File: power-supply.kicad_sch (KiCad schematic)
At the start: 17 parts, among them Q1 SIA906EDJ-T1-GE3, U3 ADP5054ACPZ-R7, U4 ADP5050ACPZ-R7

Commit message: FPGA power supply WIP
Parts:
- added C?: C_22u_0603, antmicro-footprints:0603-cap, symbol antmicroCapacitors0603:C_22u_0603
- added C?: C_100n_0402, antmicro-footprints:0402-cap, symbol antmicroCapacitors0402:C_100n_0402
- added L?: XFL4020-472MEC, antmicro-footprints:XFL4020-102MEB, symbol antmicroFixedInductors:XFL4020-472MEC
- added R?: R_100k_0402, antmicro-footprints:0402-res, symbol antmicroResistors0402:R_100k_0402
- added R?: R_2k55_0402, antmicro-footprints:0402-res, symbol antmicroResistors0402:R_2k55_0402
- added R?: R_10k2_0402, antmicro-footprints:0402-res, symbol antmicroResistors0402:R_10k2_0402
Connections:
- net GND: now also U4.11 (PGND4), U4.2 (PGND3), U4.30 (PGND), U4.HTAB (EPAD), C?.2, R?.1
- net at U4.10 (SW4): now also C?.1, L?.1 (P)
- net at U4.12 (BST4): now also C?.2
- net at U4.16 (FB4): now also R?.2, R?.2
- new net: C?.1, L?.2 (P), R?.1
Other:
- moved on the sheet: U3

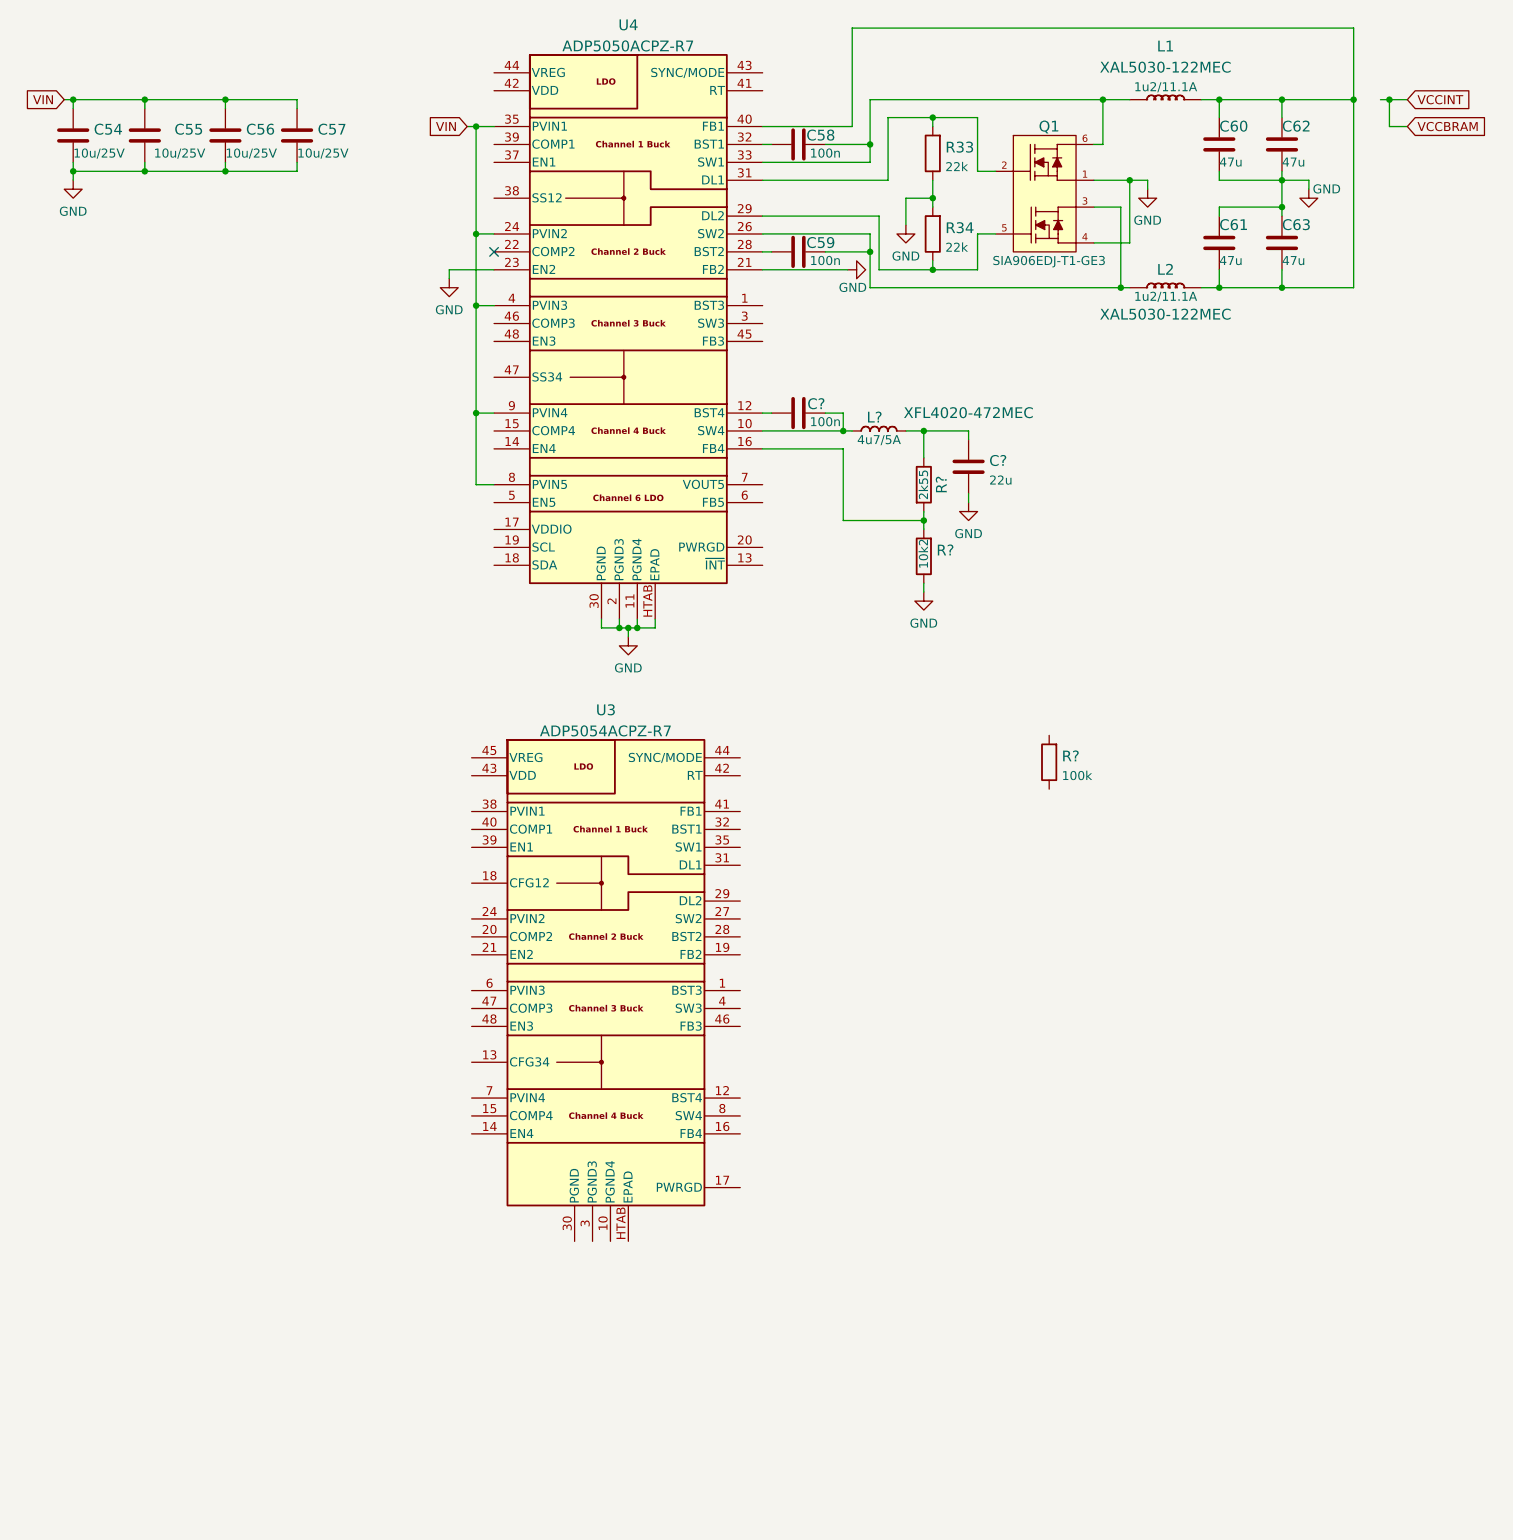
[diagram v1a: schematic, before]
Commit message: Add FPGA planar decoupling, finish DC-DC for 1V2, 1V35, 1V8, 3V3 and MGTAVCC rails
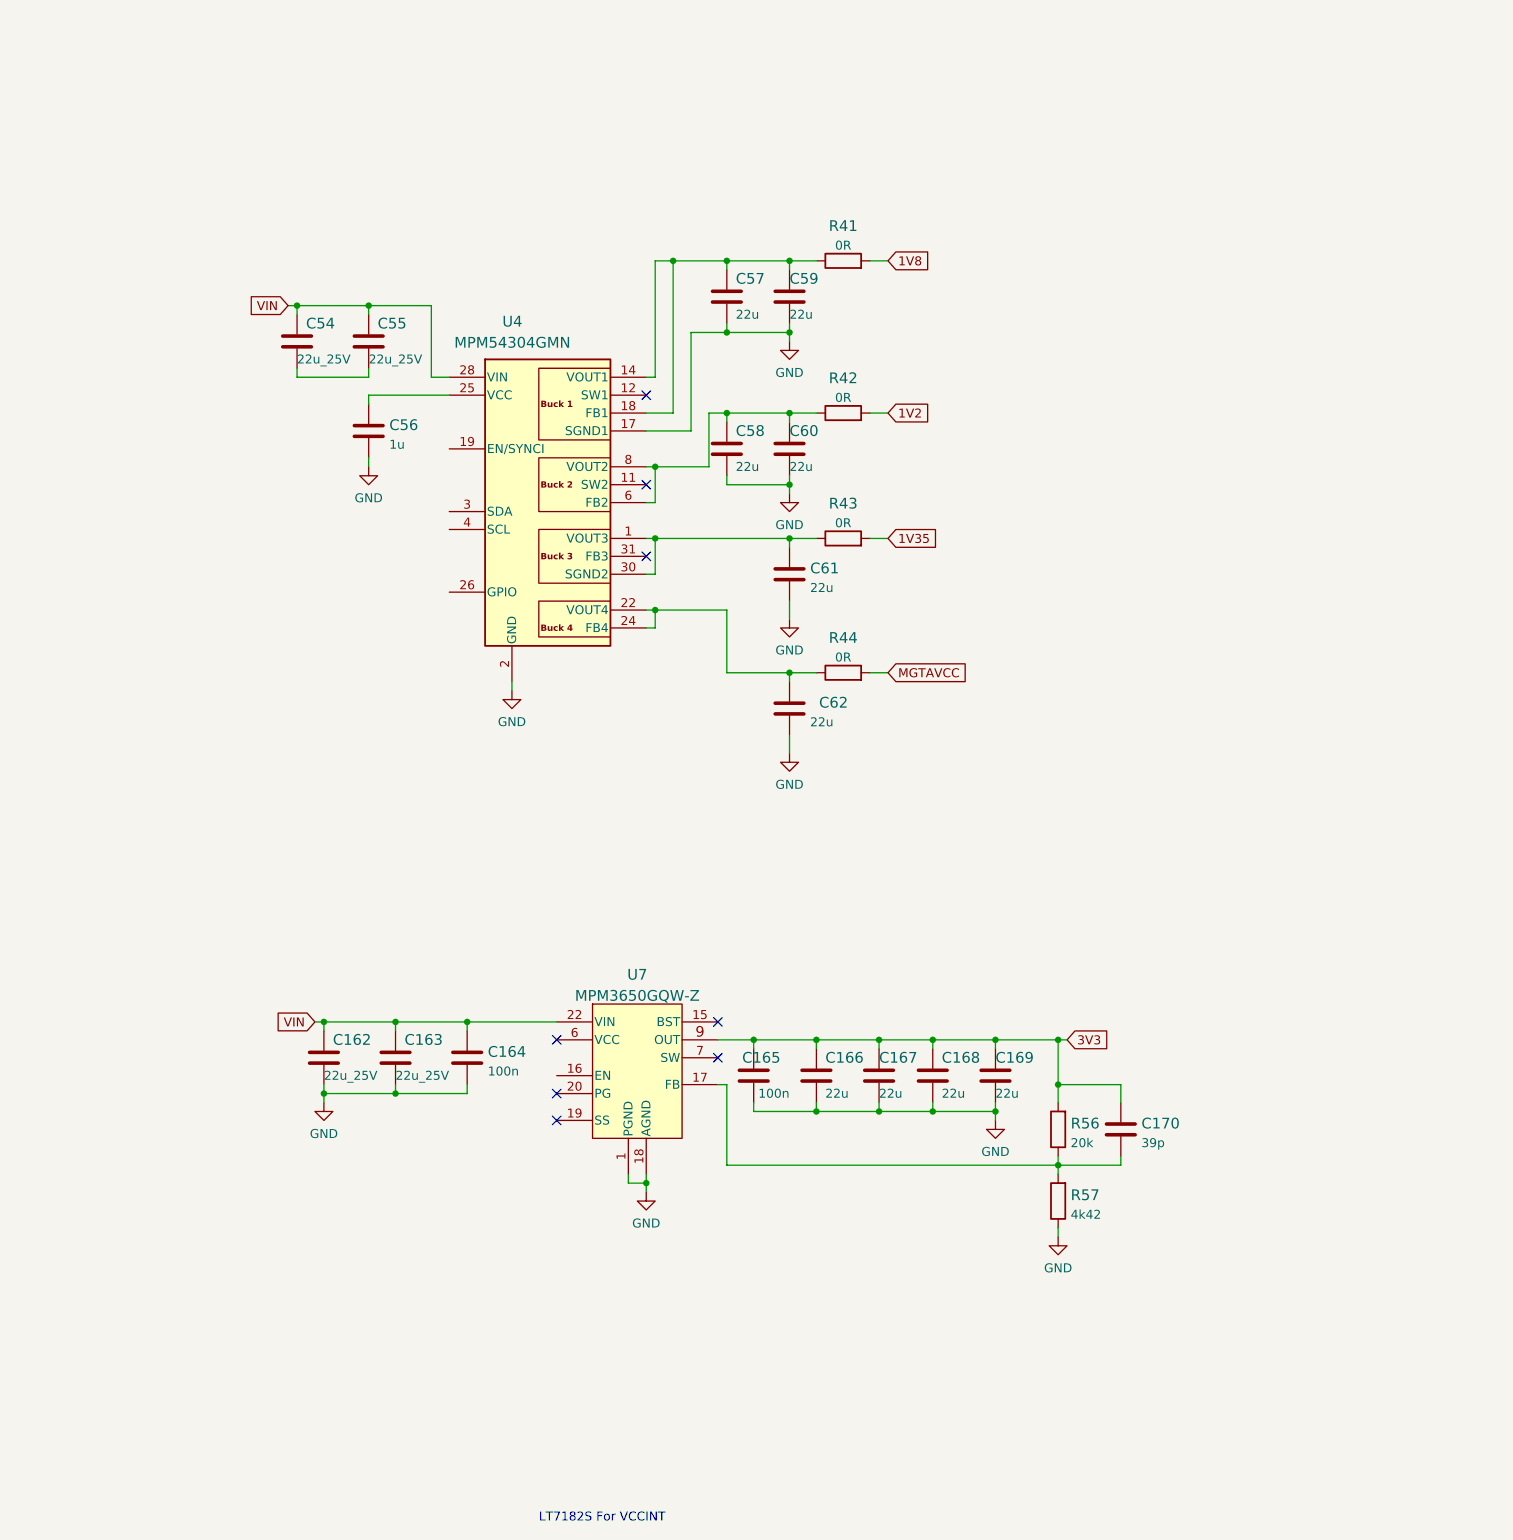
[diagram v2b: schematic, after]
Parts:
- removed C54, C55, C56, C57: C_10u_25V_0603, antmicro-footprints:0603-cap, symbol antmicroCapacitors0603:C_10u_25V_0603
- removed C58, C59, C?: C_100n_0402, antmicro-footprints:0402-cap, symbol antmicroCapacitors0402:C_100n_0402
- removed C60, C61, C62, C63: C_47u_0603, antmicro-footprints:0603-cap, symbol antmicroCapacitors0603:C_47u_0603
- removed C?: C_22u_0603, antmicro-footprints:0603-cap, symbol antmicroCapacitors0603:C_22u_0603
- removed L1, L2: XAL5030-122MEC, antmicro-footprints:Coilcraft-XAL5030, symbol antmicroFixedInductors:XAL5030-122MEC
- removed L?: XFL4020-472MEC, antmicro-footprints:XFL4020-102MEB, symbol antmicroFixedInductors:XFL4020-472MEC
- removed Q1: SIA906EDJ-T1-GE3, antmicro-footprints:VISHAY_PowerPAK_SC70-6L, symbol antmicroTransistorsFETsMOSFETsArrays:SIA906EDJ-T1-GE3
- removed R33, R34: R_22k_0402, antmicro-footprints:0402-res, symbol antmicroResistors0402:R_22k_0402
- removed R?: R_100k_0402, antmicro-footprints:0402-res, symbol antmicroResistors0402:R_100k_0402
- removed R?: R_2k55_0402, antmicro-footprints:0402-res, symbol antmicroResistors0402:R_2k55_0402
- removed R?: R_10k2_0402, antmicro-footprints:0402-res, symbol antmicroResistors0402:R_10k2_0402
- removed U3: ADP5054ACPZ-R7, antmicro-footprints:Analog_CP_48_13, symbol antmicroPMICVoltageRegulatorsDCDCSwitchingRegulators:ADP5054ACPZ-R7
- removed U4: ADP5050ACPZ-R7, antmicro-footprints:Analog_CP_48_13, symbol antmicroPMICVoltageRegulatorsDCDCSwitchingRegulators:ADP5050ACPZ-R7
- added C162, C163, C54, C55: C_22u_0805_25V, antmicro-footprints:0805-cap, symbol antmicroCapacitorsmisc:C_22u_0805_25V
- added C164, C165: C_100n_0402, antmicro-footprints:0402-cap, symbol antmicroCapacitors0402:C_100n_0402
- added C166, C167, C168, C169, C57, C58, C59, C60, C61, C62: C_22u_0603, antmicro-footprints:0603-cap, symbol antmicroCapacitors0603:C_22u_0603
- added C170: C_39p_0402, antmicro-footprints:0402-cap, symbol antmicroCapacitors0402:C_39p_0402
- added C56: C_1u_0402, antmicro-footprints:0402-cap, symbol antmicroCapacitors0402:C_1u_0402
- added R41, R42, R43, R44: R_0R_0805, antmicro-footprints:0805-res, symbol antmicroResistorsmisc:R_0R_0805
- added R56: R_20k_0402, antmicro-footprints:0402-res, symbol antmicroResistors0402:R_20k_0402
- added R57: R_4k42_0402, antmicro-footprints:0402-res, symbol antmicroResistors0402:R_4k42_0402
- added U4: MPM54304GMN, antmicro-footprints:MPS_LGA-33, symbol antmicroPMICVoltageRegulatorsDCDCSwitchingRegulators:MPM54304GMN
- added U7: MPM3650GQW-Z, antmicro-footprints:MPS_QFN24, symbol antmicroPMICVoltageRegulatorsDCDCSwitchingRegulators:MPM3650GQW-Z
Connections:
- net GND: now also C162.2, C163.2, C164.2, C165.2, C166.2, C167.2, C168.2, C169.2, C56.2, C57.2, C58.2, C59.2, C60.2, C61.2, C62.2, R57.1, U4.10 (GND), U4.13 (GND), U4.16 (GND), U4.17 (SGND1), U4.2 (GND), U4.20 (GND), U4.21 (GND), U4.27 (GND), U4.33 (GND), U4.5 (GND), U4.7 (GND), U7.1 (PGND), U7.18 (AGND), U7.2 (PGND), U7.24 (PGND), U7.3 (PGND), U7.4 (PGND), U7.5 (PGND)
- net VIN: now also C162.1, C163.1, C164.1, C54.1, C55.1, U4.28 (VIN), U4.29 (VIN), U7.22 (VIN)
- new net: C61.1, R43.1, U4.1 (VOUT3), U4.30 (SGND2), U4.32 (VOUT3)
- new net: C56.1, U4.25 (VCC)
- new net: C170.2, R56.1, R57.2, U7.17 (FB)
- new net: U7.13 (SW), U7.14 (SW), U7.23 (SW), U7.7 (SW), U7.8 (SW)
- new net: U7.20 (PG), U7.21 (PG)
- new net: C54.2, C55.2
- new net 1V2: R42.2
- new net 1V35: R43.2
- new net 1V8: R41.2
- new net 3V3: C165.1, C166.1, C167.1, C168.1, C169.1, C170.1, R56.2, U7.10 (OUT), U7.11 (OUT), U7.12 (OUT), U7.9 (OUT)
- new net MGTAVCC: R44.2
- new net VOUT1: C57.1, C59.1, R41.1, U4.14 (VOUT1), U4.15 (VOUT1), U4.18 (FB1)
- new net VOUT2: C58.1, C60.1, R42.1, U4.6 (FB2), U4.8 (VOUT2), U4.9 (VOUT2)
- new net VOUT4: C62.1, R44.1, U4.22 (VOUT4), U4.23 (VOUT4), U4.24 (FB4)
- no-connect marks 1 -> 8
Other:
- note added: "LT7182S For VCCINT"

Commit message: Unify sheets tables, add user-gpio sheet
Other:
- title: (none) -> K410T devboard
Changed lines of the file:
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@@
 (kicad_sch (version 20211123) (generator eeschema)
   (paper "A3")
+  (title_block
+    (title "K410T devboard")
+    (date "2022-12-20")
+    (rev "0.0.99")
+  )
   (junction (at 127 97.79) (diameter 0) (color 0 0 0 0)
   )

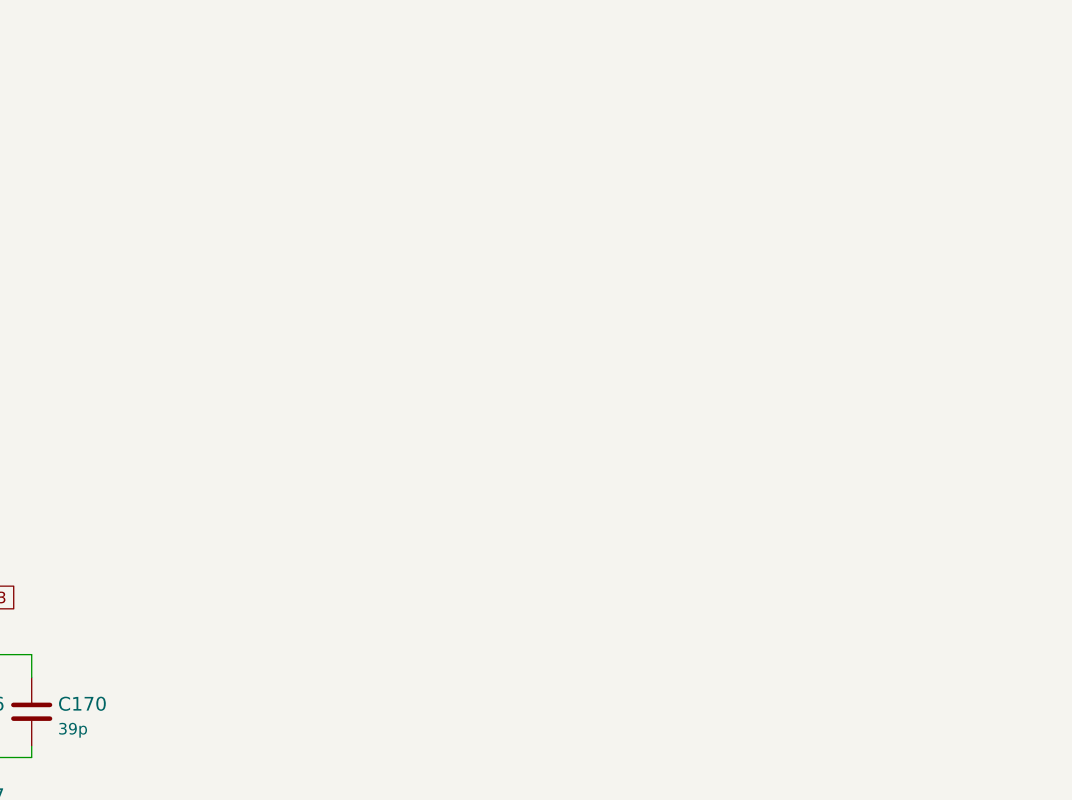
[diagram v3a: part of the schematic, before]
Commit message: Add DDR3L VTT termination regulator
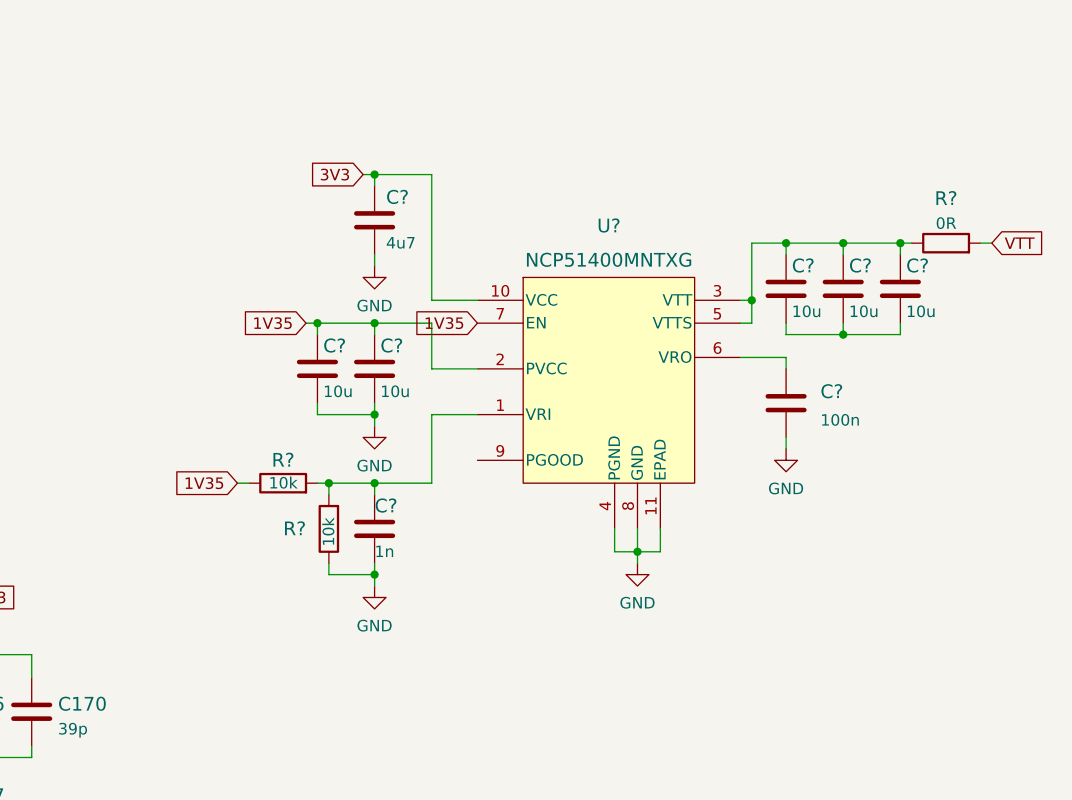
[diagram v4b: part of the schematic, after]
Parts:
- added C?: C_100n_0402, antmicro-footprints:0402-cap, symbol antmicroCapacitors0402:C_100n_0402
- added C? (x5): C_10u_0402, antmicro-footprints:0402-cap, symbol antmicroCapacitors0402:C_10u_0402
- added C?: C_4u7_0402, antmicro-footprints:0402-cap, symbol antmicroCapacitors0402:C_4u7_0402
- added C?: C_1n_0402, antmicro-footprints:0402-res, symbol antmicroCapacitors0402:C_1n_0402
- added R? (x2): R_10k_0402, antmicro-footprints:0402-res, symbol antmicroResistors0402:R_10k_0402
- added R?: R_0R_0805, antmicro-footprints:0805-res, symbol antmicroResistorsmisc:R_0R_0805
- added U?: NCP51400MNTXG, antmicro-footprints:DFN-10-1EP_3x3mm, symbol antmicroPMICVoltageRegulatorsDCDCSwitchingControllers:NCP51400MNTXG
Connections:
- net 1V35: now also C?.1, C?.1, R?.1, U?.2 (PVCC), U?.7 (EN)
- net 3V3: now also C?.1, U?.10 (VCC)
- net GND: now also C?.2, C?.2, C?.2, C?.2, C?.2, R?.1, U?.11 (EPAD), U?.4 (PGND), U?.8 (GND)
- new net: C?.1, U?.6 (VRO)
- new net: C?.1, R?.2, R?.2, U?.1 (VRI)
- new net: C?.1, C?.1, C?.1, R?.1, U?.3 (VTT), U?.5 (VTTS)
- new net: C?.2, C?.2, C?.2
- new net VTT: R?.2
